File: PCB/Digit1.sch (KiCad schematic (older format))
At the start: 29 parts

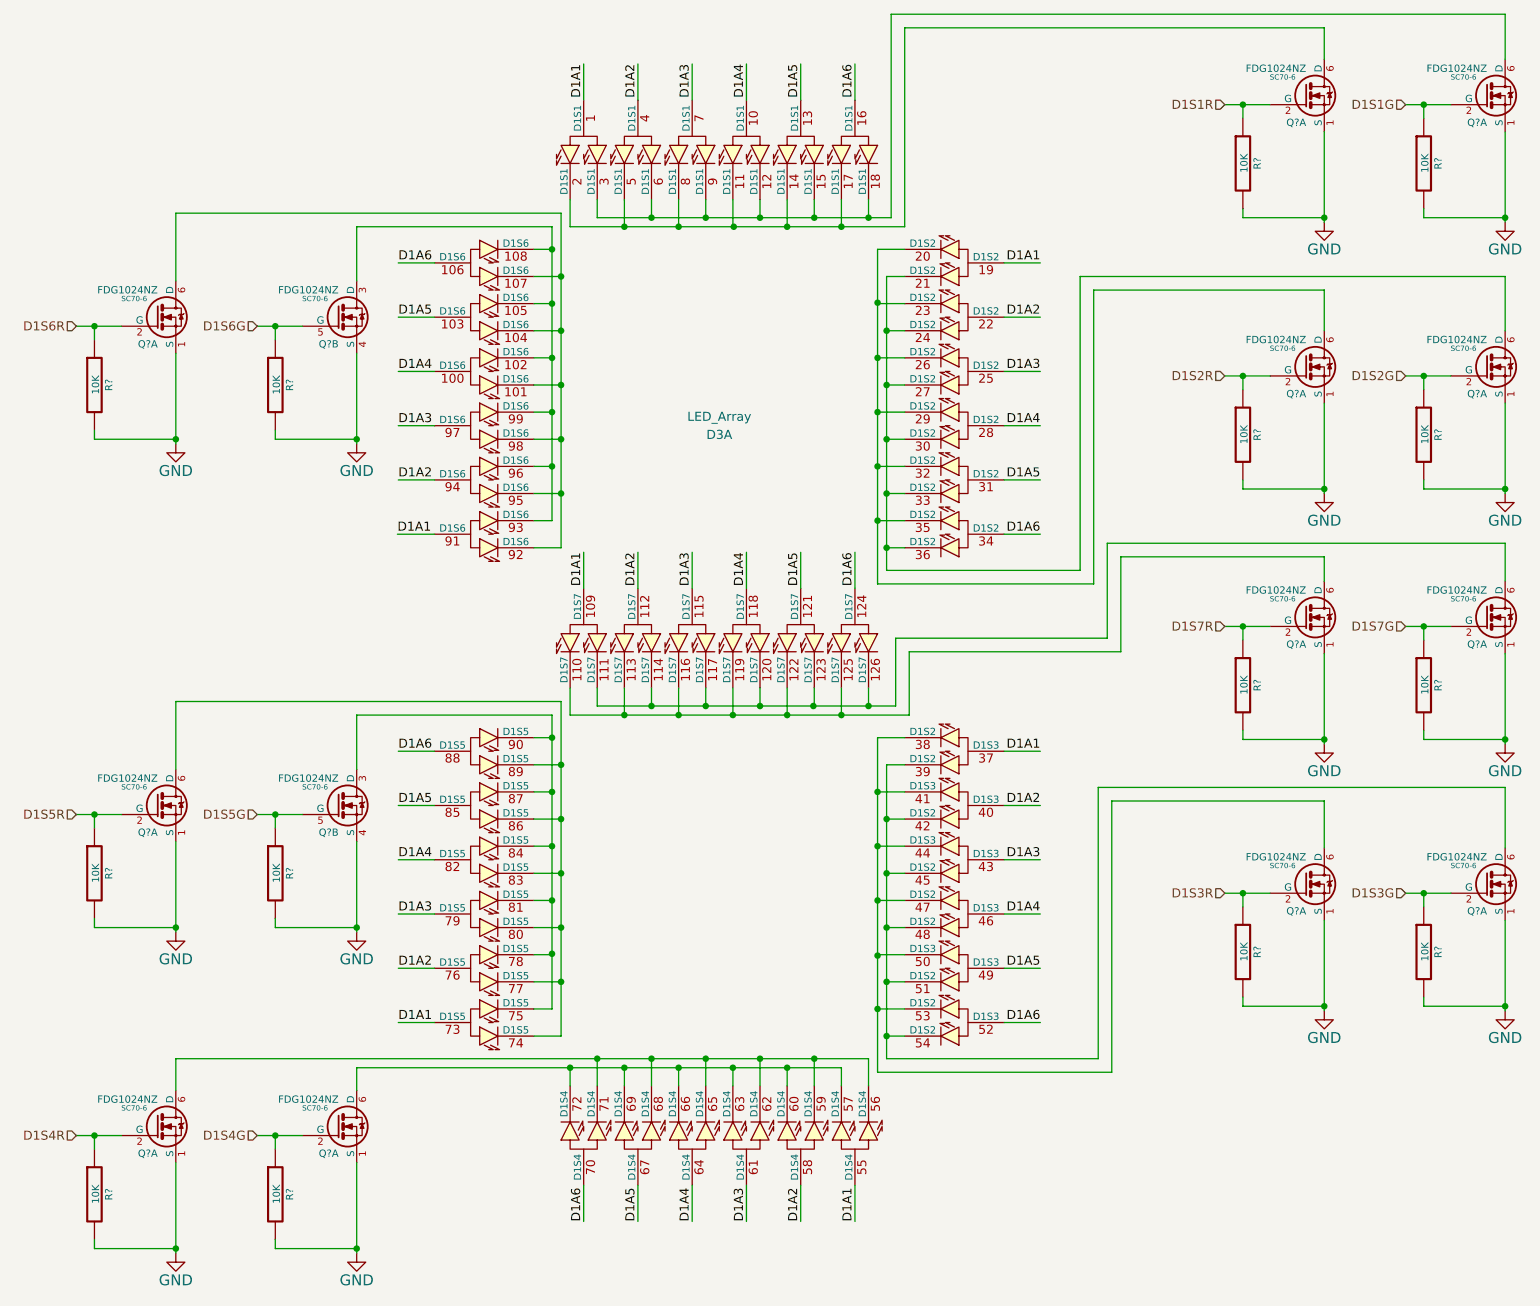
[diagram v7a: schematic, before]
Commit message: Updated mosfets.
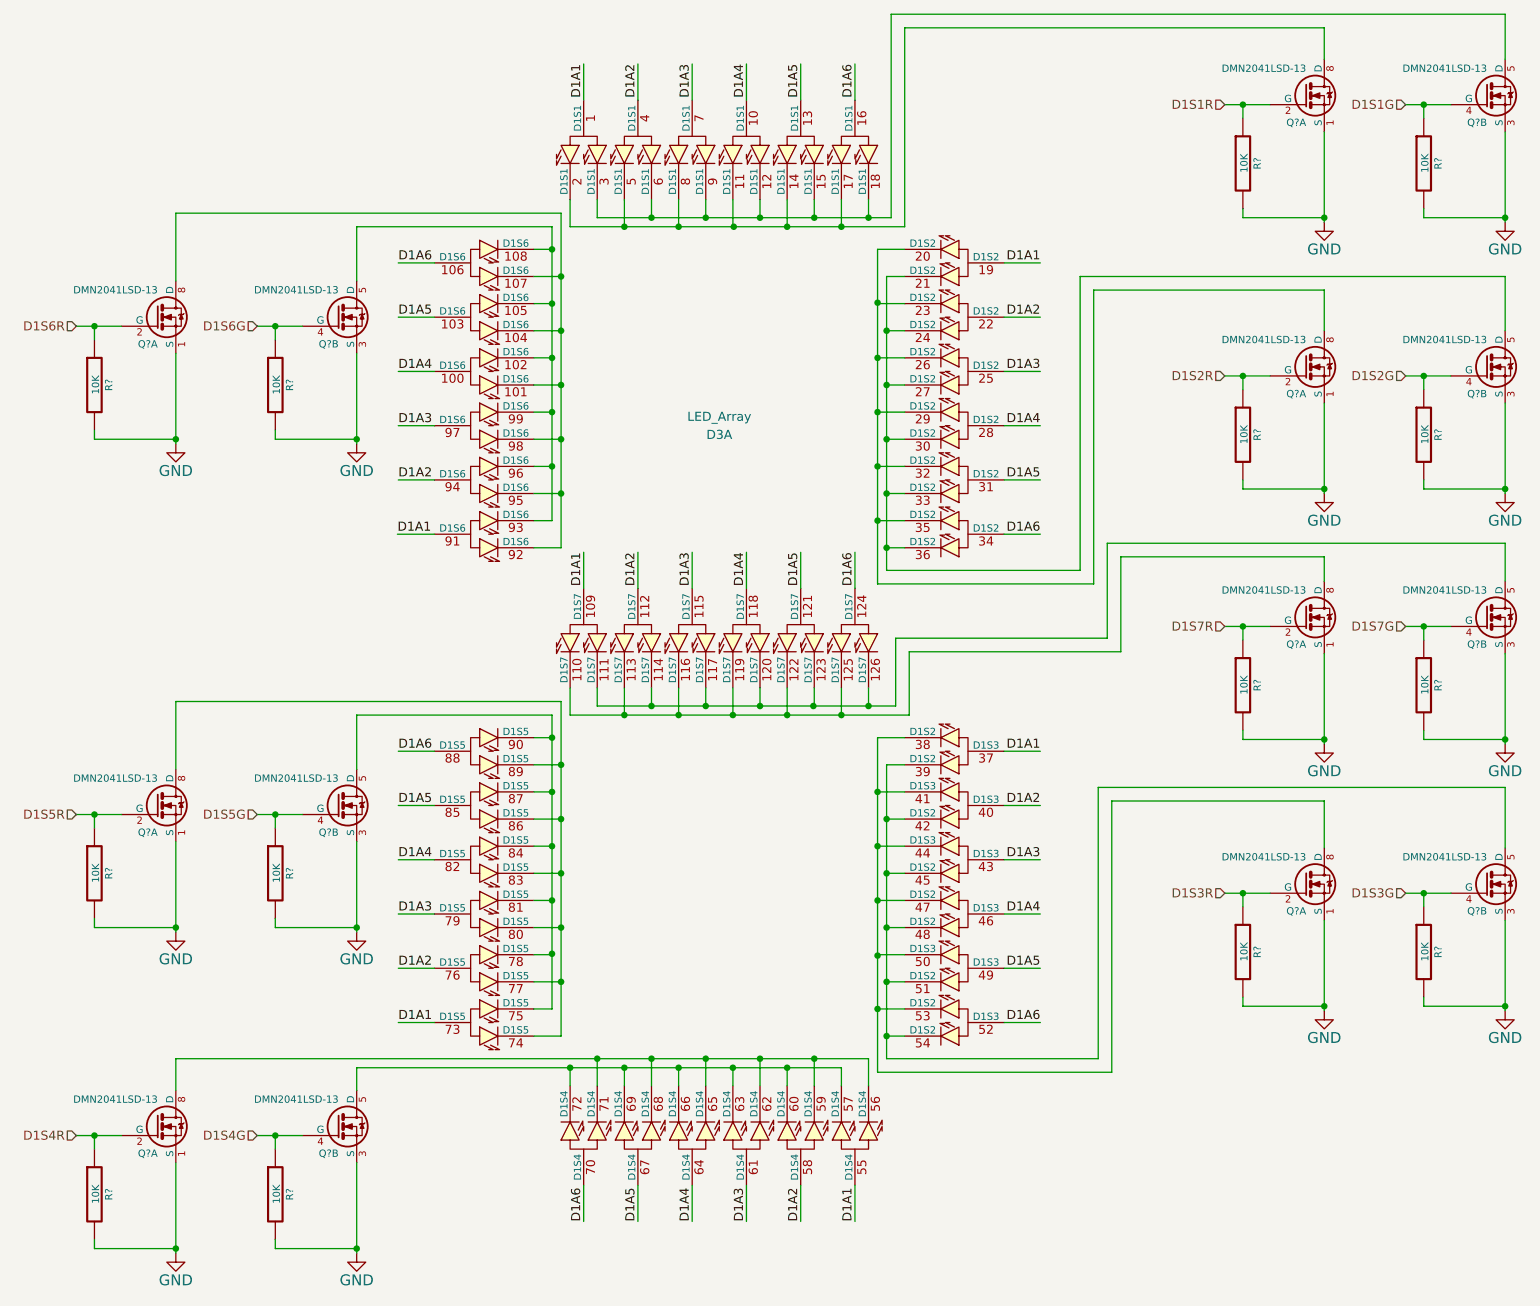
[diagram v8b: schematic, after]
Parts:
- removed Q? (x14): FDG1024NZ, SC70-6, symbol FDG1024NZ
- added Q? (x14): DMN2041LSD-13, SO-8, symbol DMN2041LSD-13
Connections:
- net D1S1G: now also Q?.4 (G)
- net D1S1R: now also Q?.2 (G)
- net D1S2G: now also Q?.4 (G)
- net D1S2R: now also Q?.2 (G)
- net D1S3G: now also Q?.4 (G)
- net D1S3R: now also Q?.2 (G)
- net D1S4G: now also Q?.4 (G)
- net D1S4R: now also Q?.2 (G)
- net D1S5G: now also Q?.4 (G)
- net D1S5R: now also Q?.2 (G)
- net D1S6G: now also Q?.4 (G)
- net D1S6R: now also Q?.2 (G)
- net D1S7G: now also Q?.4 (G)
- net D1S7R: now also Q?.2 (G)
- net GND: now also Q?.1 (S), Q?.1 (S), Q?.1 (S), Q?.1 (S), Q?.1 (S), Q?.1 (S), Q?.1 (S), Q?.3 (S), Q?.3 (S), Q?.3 (S), Q?.3 (S), Q?.3 (S), Q?.3 (S), Q?.3 (S)
- net at D3.101 (D1S6), D3.104 (D1S6), D3.107 (D1S6)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: now also Q?.8 (D)
- net at D3.102 (D1S6), D3.105 (D1S6), D3.108 (D1S6)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: now also Q?.5 (D)
- net at D3.11 (D1S1), D3.14 (D1S1), D3.17 (D1S1)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: now also Q?.8 (D)
- net at D3.110 (D1S7), D3.113 (D1S7), D3.116 (D1S7)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: now also Q?.8 (D)
- net at D3.111 (D1S7), D3.114 (D1S7), D3.117 (D1S7)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: now also Q?.5 (D)
- net at D3.12 (D1S1), D3.15 (D1S1), D3.18 (D1S1)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: now also Q?.5 (D)
- net at D3.20 (D1S2), D3.23 (D1S2), D3.26 (D1S2)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: now also Q?.8 (D)
- net at D3.21 (D1S2), D3.24 (D1S2), D3.27 (D1S2)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: now also Q?.5 (D)
- net at D3.38 (D1S2), D3.41 (D1S3), D3.44 (D1S3)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: now also Q?.8 (D)
- net at D3.39 (D1S2), D3.42 (D1S2), D3.45 (D1S2)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: now also Q?.5 (D)
- net at D3.56 (D1S4), D3.59 (D1S4), D3.62 (D1S4)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: now also Q?.8 (D)
- net at D3.57 (D1S4), D3.60 (D1S4), D3.63 (D1S4)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: now also Q?.5 (D)
- net at D3.74 (D1S5), D3.77 (D1S5), D3.80 (D1S5)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: now also Q?.8 (D)
- net at D3.75 (D1S5), D3.78 (D1S5), D3.81 (D1S5)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: now also Q?.5 (D)
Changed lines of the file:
@@
 D1A6
-$Comp
-L FDG1024NZ Q?
-U 1 1 54C622E0
-P 1350 2350
-F 0 "Q?" H 1350 2201 40  0000 R CNN
-F 1 "FDG1024NZ" H 1350 2500 40  0000 R CNN
-F 2 "SC70-6" H 1220 2452 29  0000 C CNN
-F 3 "" H 1350 2350 60  0000 C CNN
-	1    1350 2350
-	1    0    0    -1
-$EndComp
-$Comp
-L FDG1024NZ Q?
-U 2 1 54C623AD
-P 2350 2350
-F 0 "Q?" H 2350 2201 40  0000 R CNN
-F 1 "FDG1024NZ" H 2350 2500 40  0000 R CNN
-F 2 "SC70-6" H 2220 2452 29  0000 C CNN
-F 3 "" H 2350 2350 60  0000 C CNN
-	2    2350 2350
-	1    0    0    -1
-$EndComp
 $Comp
 L R R?
@@
 $EndComp
 $Comp
-L FDG1024NZ Q?
-U 1 1 54C65121
-P 1350 5050
-F 0 "Q?" H 1350 4901 40  0000 R CNN
-F 1 "FDG1024NZ" H 1350 5200 40  0000 R CNN
-F 2 "SC70-6" H 1220 5152 29  0000 C CNN
-F 3 "" H 1350 5050 60  0000 C CNN
-	1    1350 5050
-	1    0    0    -1
-$EndComp
-$Comp
 L R R?
 U 1 1 54C6512D
@@
 D1S5G
 $Comp
-L FDG1024NZ Q?
-U 2 1 54C684FF
-P 2350 5050
-F 0 "Q?" H 2350 4901 40  0000 R CNN
-F 1 "FDG1024NZ" H 2350 5200 40  0000 R CNN
-F 2 "SC70-6" H 2220 5152 29  0000 C CNN
-F 3 "" H 2350 5050 60  0000 C CNN
-	2    2350 5050
-	1    0    0    -1
-$EndComp
-$Comp
-L FDG1024NZ Q?
-U 1 1 54E98BFC
-P 1350 6825
-F 0 "Q?" H 1350 6676 40  0000 R CNN
-F 1 "FDG1024NZ" H 1350 6975 40  0000 R CNN
-F 2 "SC70-6" H 1220 6927 29  0000 C CNN
-F 3 "" H 1350 6825 60  0000 C CNN
-	1    1350 6825
-	1    0    0    -1
-$EndComp
-$Comp
 L R R?
 U 1 1 54E98C02
@@
 D1S4G
 $Comp
-L FDG1024NZ Q?
-U 1 1 54E98C30
-P 2350 6825
-F 0 "Q?" H 2350 6676 40  0000 R CNN
-F 1 "FDG1024NZ" H 2350 6975 40  0000 R CNN
-F 2 "SC70-6" H 2220 6927 29  0000 C CNN
-F 3 "" H 2350 6825 60  0000 C CNN
-	1    2350 6825
-	1    0    0    -1
-$EndComp
-$Comp
 L LED_Array D3
 U 1 1 54BC75FA
@@
 	2450 6625 2450 6500
 $Comp
-L FDG1024NZ Q?
-U 1 1 54E9A808
-P 7700 1125
-F 0 "Q?" H 7700 976 40  0000 R CNN
-F 1 "FDG1024NZ" H 7700 1275 40  0000 R CNN
-F 2 "SC70-6" H 7570 1227 29  0000 C CNN
-F 3 "" H 7700 1125 60  0000 C CNN
-	1    7700 1125
-	1    0    0    -1
-$EndComp
-$Comp
 L R R?
 U 1 1 54E9A80E
@@
 Text HLabel 8250 1175 0    50   Input ~ 0
 D1S1G
-$Comp
-L FDG1024NZ Q?
-U 1 1 54E9A828
-P 8700 1125
-F 0 "Q?" H 8700 976 40  0000 R CNN
-F 1 "FDG1024NZ" H 8700 1275 40  0000 R CNN
-F 2 "SC70-6" H 8570 1227 29  0000 C CNN
-F 3 "" H 8700 1125 60  0000 C CNN
-	1    8700 1125
-	1    0    0    -1
-$EndComp
 Wire Wire Line
 	8250 1175 8500 1175
@@
 Wire Wire Line
 	8800 675  8800 925
-$Comp
-L FDG1024NZ Q?
-U 1 1 54E9ABDF
-P 7700 2625
-F 0 "Q?" H 7700 2476 40  0000 R CNN
-F 1 "FDG1024NZ" H 7700 2775 40  0000 R CNN
-F 2 "SC70-6" H 7570 2727 29  0000 C CNN
-F 3 "" H 7700 2625 60  0000 C CNN
-	1    7700 2625
-	1    0    0    -1
-$EndComp
 $Comp
 L R R?
@@
 Text HLabel 8250 2675 0    50   Input ~ 0
 D1S2G
-$Comp
-L FDG1024NZ Q?
-U 1 1 54E9ABFF
-P 8700 2625
-F 0 "Q?" H 8700 2476 40  0000 R CNN
-F 1 "FDG1024NZ" H 8700 2775 40  0000 R CNN
-F 2 "SC70-6" H 8570 2727 29  0000 C CNN
-F 3 "" H 8700 2625 60  0000 C CNN
-	1    8700 2625
-	1    0    0    -1
-$EndComp
 Wire Wire Line
 	8250 2675 8500 2675
@@
 Wire Wire Line
 	8800 2125 8800 2425
-$Comp
-L FDG1024NZ Q?
-U 1 1 54E9AD9A
-P 7700 5485
-F 0 "Q?" H 7700 5336 40  0000 R CNN
-F 1 "FDG1024NZ" H 7700 5635 40  0000 R CNN
-F 2 "SC70-6" H 7570 5587 29  0000 C CNN
-F 3 "" H 7700 5485 60  0000 C CNN
-	1    7700 5485
-	1    0    0    -1
-$EndComp
 $Comp
 L R R?
@@
 Text HLabel 8250 5535 0    50   Input ~ 0
 D1S3G
-$Comp
-L FDG1024NZ Q?
-U 1 1 54E9ADBA
-P 8700 5485
-F 0 "Q?" H 8700 5336 40  0000 R CNN
-F 1 "FDG1024NZ" H 8700 5635 40  0000 R CNN
-F 2 "SC70-6" H 8570 5587 29  0000 C CNN
-F 3 "" H 8700 5485 60  0000 C CNN
-	1    8700 5485
-	1    0    0    -1
-$EndComp
 Wire Wire Line
 	8250 5535 8500 5535
@@
 Wire Wire Line
 	7800 750  7800 925
-$Comp
-L FDG1024NZ Q?
-U 1 1 54E9E0B4
-P 7700 4010
-F 0 "Q?" H 7700 3861 40  0000 R CNN
-F 1 "FDG1024NZ" H 7700 4160 40  0000 R CNN
-F 2 "SC70-6" H 7570 4112 29  0000 C CNN
-F 3 "" H 7700 4010 60  0000 C CNN
-	1    7700 4010
-	1    0    0    -1
-$EndComp
 $Comp
 L R R?
@@
 Text HLabel 8250 4060 0    50   Input ~ 0
 D1S7G
-$Comp
-L FDG1024NZ Q?
-U 1 1 54E9E0D4
-P 8700 4010
-F 0 "Q?" H 8700 3861 40  0000 R CNN
-F 1 "FDG1024NZ" H 8700 4160 40  0000 R CNN
-F 2 "SC70-6" H 8570 4112 29  0000 C CNN
-F 3 "" H 8700 4010 60  0000 C CNN
-	1    8700 4010
-	1    0    0    -1
-$EndComp
 Wire Wire Line
 	8250 4060 8500 4060
@@
 EndData
 $EndBitmap
+$Comp
+L DMN2041LSD-13 Q?
+U 1 1 54ED6F68
+P 1350 2350
+F 0 "Q?" H 1350 2201 40  0000 R CNN
+F 1 "DMN2041LSD-13" H 1350 2500 40  0000 R CNN
+F 2 "SO-8" H 1220 2452 29  0001 C CNN
+F 3 "" H 1350 2350 60  0000 C CNN
+	1    1350 2350
+	1    0    0    -1
+$EndComp
+$Comp
+L DMN2041LSD-13 Q?
+U 2 1 54ED6FF7
+P 2350 2350
+F 0 "Q?" H 2350 2201 40  0000 R CNN
+F 1 "DMN2041LSD-13" H 2350 2500 40  0000 R CNN
+F 2 "SO-8" H 2220 2452 29  0001 C CNN
+F 3 "" H 2350 2350 60  0000 C CNN
+	2    2350 2350
+	1    0    0    -1
+$EndComp
+$Comp
+L DMN2041LSD-13 Q?
+U 1 1 54ED73EF
+P 1350 5050
+F 0 "Q?" H 1350 4901 40  0000 R CNN
+F 1 "DMN2041LSD-13" H 1350 5200 40  0000 R CNN
+F 2 "SO-8" H 1220 5152 29  0001 C CNN
+F 3 "" H 1350 5050 60  0000 C CNN
+	1    1350 5050
+	1    0    0    -1
+$EndComp
+$Comp
+L DMN2041LSD-13 Q?
+U 2 1 54ED7454
+P 2350 5050
+F 0 "Q?" H 2350 4901 40  0000 R CNN
+F 1 "DMN2041LSD-13" H 2350 5200 40  0000 R CNN
+F 2 "SO-8" H 2220 5152 29  0001 C CNN
+F 3 "" H 2350 5050 60  0000 C CNN
+	2    2350 5050
+	1    0    0    -1
+$EndComp
+$Comp
+L DMN2041LSD-13 Q?
+U 1 1 54ED788B
+P 1350 6825
+F 0 "Q?" H 1350 6676 40  0000 R CNN
+F 1 "DMN2041LSD-13" H 1350 6975 40  0000 R CNN
+F 2 "SO-8" H 1220 6927 29  0001 C CNN
+F 3 "" H 1350 6825 60  0000 C CNN
+	1    1350 6825
+	1    0    0    -1
+$EndComp
+$Comp
+L DMN2041LSD-13 Q?
+U 2 1 54ED78E8
+P 2350 6825
+F 0 "Q?" H 2350 6676 40  0000 R CNN
+F 1 "DMN2041LSD-13" H 2350 6975 40  0000 R CNN
+F 2 "SO-8" H 2220 6927 29  0001 C CNN
+F 3 "" H 2350 6825 60  0000 C CNN
+	2    2350 6825
+	1    0    0    -1
+$EndComp
+$Comp
+L DMN2041LSD-13 Q?
+U 1 1 54ED8102
+P 7700 5485
+F 0 "Q?" H 7700 5336 40  0000 R CNN
+F 1 "DMN2041LSD-13" H 7700 5635 40  0000 R CNN
+F 2 "SO-8" H 7570 5587 29  0001 C CNN
+F 3 "" H 7700 5485 60  0000 C CNN
+	1    7700 5485
+	1    0    0    -1
+$EndComp
+$Comp
+L DMN2041LSD-13 Q?
+U 2 1 54ED8163
+P 8700 5485
+F 0 "Q?" H 8700 5336 40  0000 R CNN
+F 1 "DMN2041LSD-13" H 8700 5635 40  0000 R CNN
+F 2 "SO-8" H 8570 5587 29  0001 C CNN
+F 3 "" H 8700 5485 60  0000 C CNN
+	2    8700 5485
+	1    0    0    -1
+$EndComp
+$Comp
+L DMN2041LSD-13 Q?
+U 1 1 54ED8542
+P 7700 4010
+F 0 "Q?" H 7700 3861 40  0000 R CNN
+F 1 "DMN2041LSD-13" H 7700 4160 40  0000 R CNN
+F 2 "SO-8" H 7570 4112 29  0001 C CNN
+F 3 "" H 7700 4010 60  0000 C CNN
+	1    7700 4010
+	1    0    0    -1
+$EndComp
+$Comp
+L DMN2041LSD-13 Q?
+U 2 1 54ED859D
+P 8700 4010
+F 0 "Q?" H 8700 3861 40  0000 R CNN
+F 1 "DMN2041LSD-13" H 8700 4160 40  0000 R CNN
+F 2 "SO-8" H 8570 4112 29  0001 C CNN
+F 3 "" H 8700 4010 60  0000 C CNN
+	2    8700 4010
+	1    0    0    -1
+$EndComp
+$Comp
+L DMN2041LSD-13 Q?
+U 1 1 54ED8AB2
+P 7700 2625
+F 0 "Q?" H 7700 2476 40  0000 R CNN
+F 1 "DMN2041LSD-13" H 7700 2775 40  0000 R CNN
+F 2 "SO-8" H 7570 2727 29  0001 C CNN
+F 3 "" H 7700 2625 60  0000 C CNN
+	1    7700 2625
+	1    0    0    -1
+$EndComp
+$Comp
+L DMN2041LSD-13 Q?
+U 2 1 54ED8B2B
+P 8700 2625
+F 0 "Q?" H 8700 2476 40  0000 R CNN
+F 1 "DMN2041LSD-13" H 8700 2775 40  0000 R CNN
+F 2 "SO-8" H 8570 2727 29  0001 C CNN
+F 3 "" H 8700 2625 60  0000 C CNN
+	2    8700 2625
+	1    0    0    -1
+$EndComp
+$Comp
+L DMN2041LSD-13 Q?
+U 1 1 54ED9154
+P 7700 1125
+F 0 "Q?" H 7700 976 40  0000 R CNN
+F 1 "DMN2041LSD-13" H 7700 1275 40  0000 R CNN
+F 2 "SO-8" H 7570 1227 29  0001 C CNN
+F 3 "" H 7700 1125 60  0000 C CNN
+	1    7700 1125
+	1    0    0    -1
+$EndComp
+$Comp
+L DMN2041LSD-13 Q?
+U 2 1 54ED91B9
+P 8700 1125
+F 0 "Q?" H 8700 976 40  0000 R CNN
+F 1 "DMN2041LSD-13" H 8700 1275 40  0000 R CNN
+F 2 "SO-8" H 8570 1227 29  0001 C CNN
+F 3 "" H 8700 1125 60  0000 C CNN
+	2    8700 1125
+	1    0    0    -1
+$EndComp
 $EndSCHEMATC
